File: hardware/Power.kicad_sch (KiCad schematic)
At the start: 0 parts

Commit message: Powerchain
Powerchain first draft done
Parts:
- added BT1: 4.8-6V, TerminalBlock:TerminalBlock_MaiXu_MX126-5.0-02P_1x02_P5.00mm, symbol Device:Battery
- added C10, C9: 1uF, symbol Device:C_Small_US
- added Q1: DMG2305UX, Package_TO_SOT_SMD:SOT-23, symbol Transistor_FET:DMG2301L
- added U4: S-1206B50-M3T1U, SOT-23-3_ABL:SOT-23-3_ABL, symbol S-1206B50-M3T1U:S-1206B50-M3T1U
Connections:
- new net: BT1.1 (+), C9.1, U4.1 (VIN)
- new net: C10.1, Q1.3 (D), U4.3 (VOUT)
- new net GND: BT1.2 (-), C10.2, C9.2, U4.2 (VSS)
- new net VBUS: Q1.1 (G)
- new net VSYS: Q1.2 (S)

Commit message: Added Button circuit
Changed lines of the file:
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@@
+	)
+	(junction
+		(at 50.8 53.34)
+		(diameter 0)
+		(color 0 0 0 0)
+	)
+	(junction
+		(at 50.8 66.04)
+		(diameter 0)
+		(color 0 0 0 0)
 	)
 	(junction
@@
 	(wire
 		(pts
+			(xy 50.8 53.34) (xy 50.8 50.8)
+		)
+		(stroke
+			(width 0)
+			(type default)
+		)
+	)
+	(wire
+		(pts
 			(xy 104.14 50.8) (xy 113.03 50.8)
 		)
@@
 	(wire
 		(pts
-			(xy 50.8 67.31) (xy 50.8 64.77)
+			(xy 50.8 66.04) (xy 50.8 64.77)
+		)
+		(stroke
+			(width 0)
+			(type default)
+		)
+	)
+	(wire
+		(pts
+			(xy 50.8 67.31) (xy 50.8 66.04)
 		)
 		(stroke
@@
 	(wire
 		(pts
-			(xy 50.8 54.61) (xy 50.8 50.8)
+			(xy 50.8 54.61) (xy 50.8 53.34)
 		)
 		(stroke
@@
 	)
 	(symbol
+		(lib_id "power:PWR_FLAG")
+		(at 50.8 53.34 90)
+		(unit 1)
+		(exclude_from_sim no)
+		(in_bom yes)
+		(on_board yes)
+		(dnp no)
+		(fields_autoplaced yes)
+		(property "Reference" "#FLG04"
+			(at 48.895 53.34 0)
+			(effects
+				(font
+					(size 1.27 1.27)
+				)
+				(hide yes)
+			)
+		)
+		(property "Value" "PWR_FLAG"
+			(at 46.99 53.3399 90)
+			(effects
+				(font
+					(size 1.27 1.27)
+				)
+				(justify left)
+			)
+		)
+		(property "Footprint" ""
+			(at 50.8 53.34 0)
+			(effects
+				(font
+					(size 1.27 1.27)
+				)
+				(hide yes)
+			)
+		)
+		(property "Datasheet" "~"
+			(at 50.8 53.34 0)
+			(effects
+				(font
+					(size 1.27 1.27)
+				)
+				(hide yes)
+			)
+		)
+		(property "Description" "Special symbol for telling ERC where power comes from"
+			(at 50.8 53.34 0)
+			(effects
+				(font
+					(size 1.27 1.27)
+				)
+				(hide yes)
+			)
+		)
+		(pin "1"
+		)
+		(instances
+			(project ""
+				(path "/adf646d2-aa7c-4345-9423-7107505b3b06/5cfe90a0-b8d3-442a-948b-db843cef3756"
+					(reference "#FLG04")
+					(unit 1)
+				)
+			)
+		)
+	)
+	(symbol
 		(lib_id "power:GND")
 		(at 63.5 67.31 0)
@@
 					(unit 1)
 				)
+			)
+		)
+	)
+	(symbol
+		(lib_id "power:PWR_FLAG")
+		(at 50.8 66.04 90)
+		(unit 1)
+		(exclude_from_sim no)
+		(in_bom yes)
+		(on_board yes)
+		(dnp no)
+		(fields_autoplaced yes)
+		(property "Reference" "#FLG05"
+			(at 48.895 66.04 0)
+			(effects
+				(font
+					(size 1.27 1.27)
+				)
+				(hide yes)
+			)
+		)
+		(property "Value" "PWR_FLAG"
+			(at 46.99 66.0399 90)
+			(effects
+				(font
+					(size 1.27 1.27)
+				)
+				(justify left)
+			)
+		)
+		(property "Footprint" ""
+			(at 50.8 66.04 0)
+			(effects
+				(font
+					(size 1.27 1.27)
+				)
+				(hide yes)
+			)
+		)
+		(property "Datasheet" "~"
+			(at 50.8 66.04 0)
+			(effects
+				(font
+					(size 1.27 1.27)
+				)
+				(hide yes)
+			)
+		)
+		(property "Description" "Special symbol for telling ERC where power comes from"
+			(at 50.8 66.04 0)
+			(effects
+				(font
+					(size 1.27 1.27)
+				)
+				(hide yes)
+			)
+		)
+		(pin "1"
+		)
+		(instances
+			(project "Main"
+				(path "/adf646d2-aa7c-4345-9423-7107505b3b06/5cfe90a0-b8d3-442a-948b-db843cef3756"
+					(reference "#FLG05")
+					(unit 1)
+				)

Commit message: Rough Board Layout
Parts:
- C10, C9: footprint (none) -> Capacitor_SMD:C_1812_4532Metric
- U4: footprint SOT-23-3_ABL:SOT-23-3_ABL -> Package_TO_SOT_SMD:SOT-23-3
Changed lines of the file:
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@@
 			)
 		)
-		(property "Footprint" "SOT-23-3_ABL:SOT-23-3_ABL"
+		(property "Footprint" "Package_TO_SOT_SMD:SOT-23-3"
 			(at 63.5 50.8 0)
 			(effects
@@
 			)
 		)
-		(property "Footprint" ""
+		(property "Footprint" "Capacitor_SMD:C_1812_4532Metric"
 			(at 113.03 60.96 0)
 			(effects
@@
 			)
 		)
-		(property "Footprint" ""
+		(property "Footprint" "Capacitor_SMD:C_1812_4532Metric"
 			(at 63.5 60.96 0)
 			(effects

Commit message: Reduced Component Sizes + Added Mounting Holes
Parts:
- C10, C9: footprint Capacitor_SMD:C_1812_4532Metric -> Capacitor_SMD:C_1206_3216Metric
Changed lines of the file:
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@@
 			)
 		)
-		(property "Footprint" "Capacitor_SMD:C_1812_4532Metric"
+		(property "Footprint" "Capacitor_SMD:C_1206_3216Metric"
 			(at 113.03 60.96 0)
 			(effects
@@
 			)
 		)
-		(property "Footprint" "Capacitor_SMD:C_1812_4532Metric"
+		(property "Footprint" "Capacitor_SMD:C_1206_3216Metric"
 			(at 63.5 60.96 0)
 			(effects

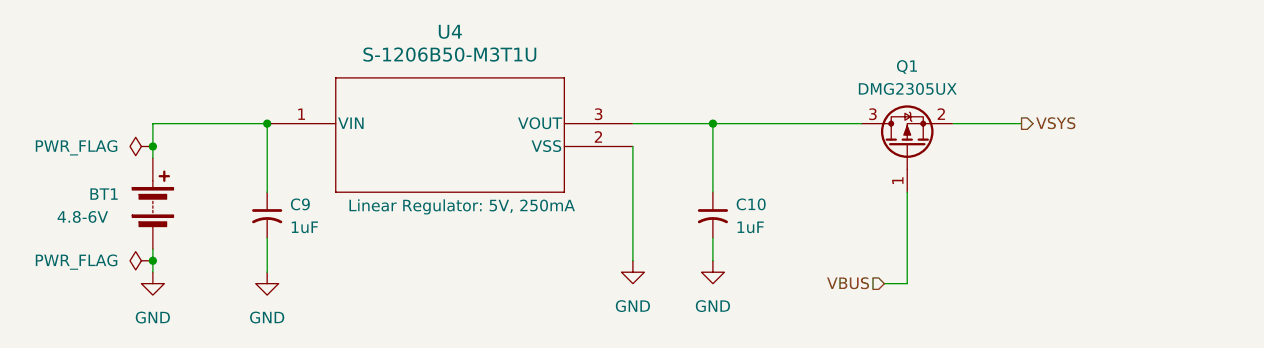
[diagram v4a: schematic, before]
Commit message: PWM Audio, Power fix
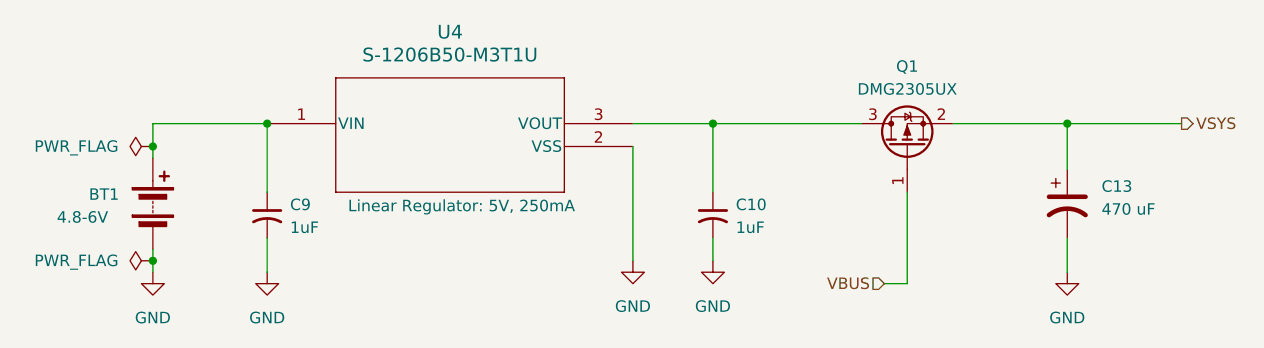
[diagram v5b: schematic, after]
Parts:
- added C13: 470 uF, symbol Device:C_Polarized_US
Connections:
- net GND: now also C13.2
- net VSYS: now also C13.1
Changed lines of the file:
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@@
+	)
+	(junction
+		(at 152.4 50.8)
+		(diameter 0)
+		(color 0 0 0 0)
 	)
 	(junction
@@
 	(wire
 		(pts
+			(xy 152.4 55.88) (xy 152.4 50.8)
+		)
+		(stroke
+			(width 0)
+			(type default)
+		)
+	)
+	(wire
+		(pts
+			(xy 152.4 67.31) (xy 152.4 63.5)
+		)
+		(stroke
+			(width 0)
+			(type default)
+		)
+	)
+	(wire
+		(pts
 			(xy 63.5 50.8) (xy 63.5 58.42)
 		)
@@
 	(wire
 		(pts
+			(xy 152.4 50.8) (xy 139.7 50.8)
+		)
+		(stroke
+			(width 0)
+			(type default)
+		)
+	)
+	(wire
+		(pts
 			(xy 113.03 50.8) (xy 113.03 58.42)
 		)
@@
 	(wire
 		(pts
-			(xy 147.32 50.8) (xy 139.7 50.8)
+			(xy 165.1 50.8) (xy 152.4 50.8)
 		)
 		(stroke
@@
 	(hierarchical_label "VSYS"
 		(shape output)
-		(at 147.32 50.8 0)
+		(at 165.1 50.8 0)
 		(effects
 			(font
@@
 			)
 			(justify left)
+		)
+	)
+	(symbol
+		(lib_id "Device:C_Polarized_US")
+		(at 152.4 59.69 0)
+		(unit 1)
+		(exclude_from_sim no)
+		(in_bom yes)
+		(on_board yes)
+		(dnp no)
+		(fields_autoplaced yes)
+		(property "Reference" "C13"
+			(at 156.21 57.7849 0)
+			(effects
+				(font
+					(size 1.27 1.27)
+				)
+				(justify left)
+			)
+		)
+		(property "Value" "470 uF"
+			(at 156.21 60.3249 0)
+			(effects
+				(font
+					(size 1.27 1.27)
+				)
+				(justify left)
+			)
+		)
+		(property "Footprint" ""
+			(at 152.4 59.69 0)
+			(effects
+				(font
+					(size 1.27 1.27)
+				)
+				(hide yes)
+			)
+		)
+		(property "Datasheet" "~"
+			(at 152.4 59.69 0)
+			(effects
+				(font
+					(size 1.27 1.27)
+				)
+				(hide yes)
+			)
+		)
+		(property "Description" "Polarized capacitor, US symbol"
+			(at 152.4 59.69 0)
+			(effects
+				(font
+					(size 1.27 1.27)
+				)
+				(hide yes)
+			)
+		)
+		(pin "1"
+		)
+		(pin "2"
+		)
+		(instances
+			(project ""
+				(path "/adf646d2-aa7c-4345-9423-7107505b3b06/5cfe90a0-b8d3-442a-948b-db843cef3756"
+					(reference "C13")
+					(unit 1)
+				)
+			)
 		)
 	)
@@
 					(unit 1)
 				)
+			)
+		)
+	)
+	(symbol
+		(lib_id "power:GND")
+		(at 152.4 67.31 0)
+		(unit 1)
+		(exclude_from_sim no)
+		(in_bom yes)
+		(on_board yes)
+		(dnp no)
+		(fields_autoplaced yes)
+		(property "Reference" "#PWR037"
+			(at 152.4 73.66 0)
+			(effects
+				(font
+					(size 1.27 1.27)
+				)
+				(hide yes)
+			)
+		)
+		(property "Value" "GND"
+			(at 152.4 72.39 0)
+			(effects
+				(font
+					(size 1.27 1.27)
+				)
+			)
+		)
+		(property "Footprint" ""
+			(at 152.4 67.31 0)
+			(effects
+				(font
+					(size 1.27 1.27)
+				)
+				(hide yes)
+			)
+		)
+		(property "Datasheet" ""
+			(at 152.4 67.31 0)
+			(effects
+				(font
+					(size 1.27 1.27)
+				)
+				(hide yes)
+			)
+		)
+		(property "Description" "Power symbol creates a global label with name \"GND\" , ground"
+			(at 152.4 67.31 0)
+			(effects
+				(font
+					(size 1.27 1.27)
+				)
+				(hide yes)
+			)
+		)
+		(pin "1"
+		)
+		(instances
+			(project ""
+				(path "/adf646d2-aa7c-4345-9423-7107505b3b06/5cfe90a0-b8d3-442a-948b-db843cef3756"
+					(reference "#PWR037")
+					(unit 1)
+				)

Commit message: Repositioned + Added volume potentiometer to PMW Audio
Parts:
- C13: footprint (none) -> Capacitor_Tantalum_SMD:CP_EIA-7343-30_AVX-N
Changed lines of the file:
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@@
 			)
 		)
-		(property "Footprint" ""
+		(property "Footprint" "Capacitor_Tantalum_SMD:CP_EIA-7343-30_AVX-N"
 			(at 152.4 59.69 0)
 			(effects

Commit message: Did it all lmao (pcb traces ready for full review)
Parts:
- BT1: value 4.8-6V -> 4 AA
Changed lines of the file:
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@@
 			)
 		)
-		(property "Value" "4.8-6V"
+		(property "Value" "4 AA"
 			(at 40.132 61.214 0)
 			(effects
@@
 		)
 		(property "Footprint" "TerminalBlock:TerminalBlock_MaiXu_MX126-5.0-02P_1x02_P5.00mm"
-			(at 50.8 58.166 90)
+			(at 25.654 56.134 90)
 			(effects
 				(font
